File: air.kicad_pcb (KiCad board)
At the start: 2 copper layers, 40.5 x 19.3 mm, 48 parts, among them J1 Conn_01x05, J2 Conn_01x05, J3 Conn_01x04, U2 AIR32F103CBT6-LQFP48, U3 RT9013-33GB, U4 USBLC6-2SC6, Y1 8M/20pF

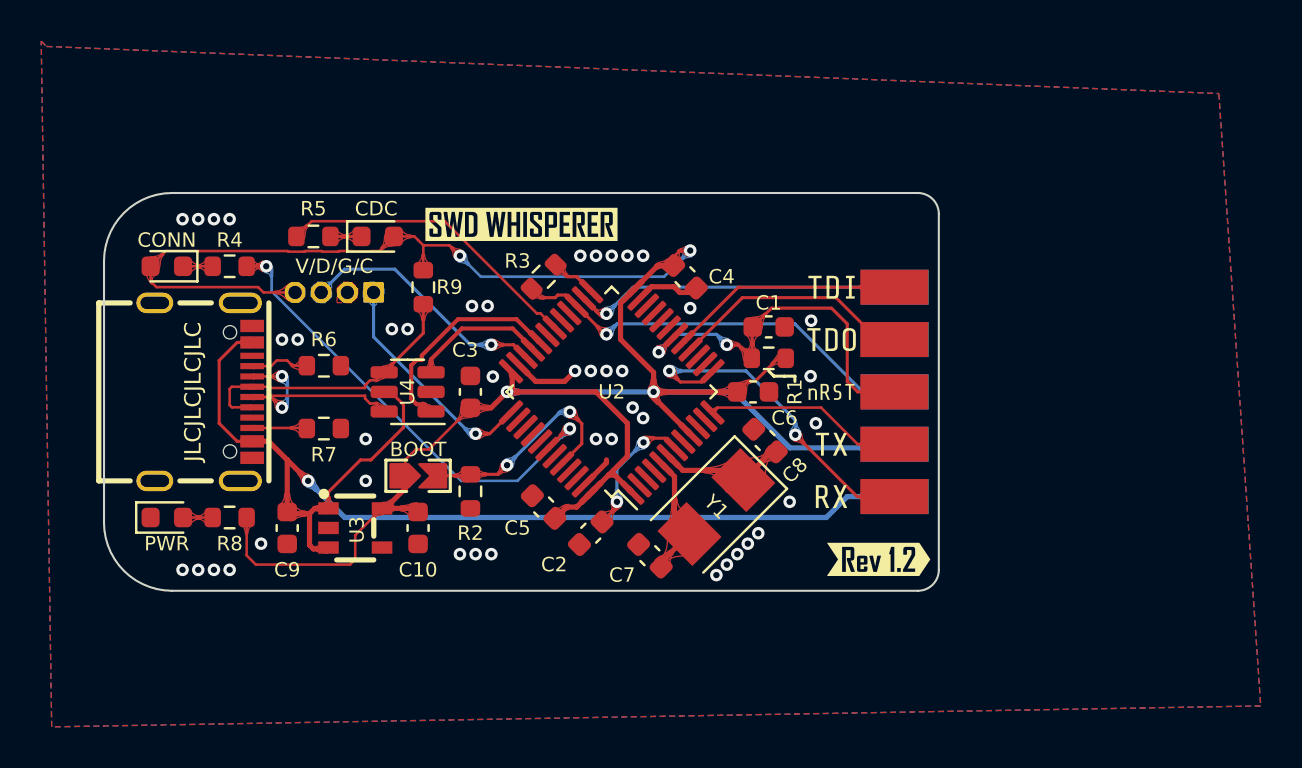
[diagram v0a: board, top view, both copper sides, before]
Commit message: V1.3 3225晶振版本
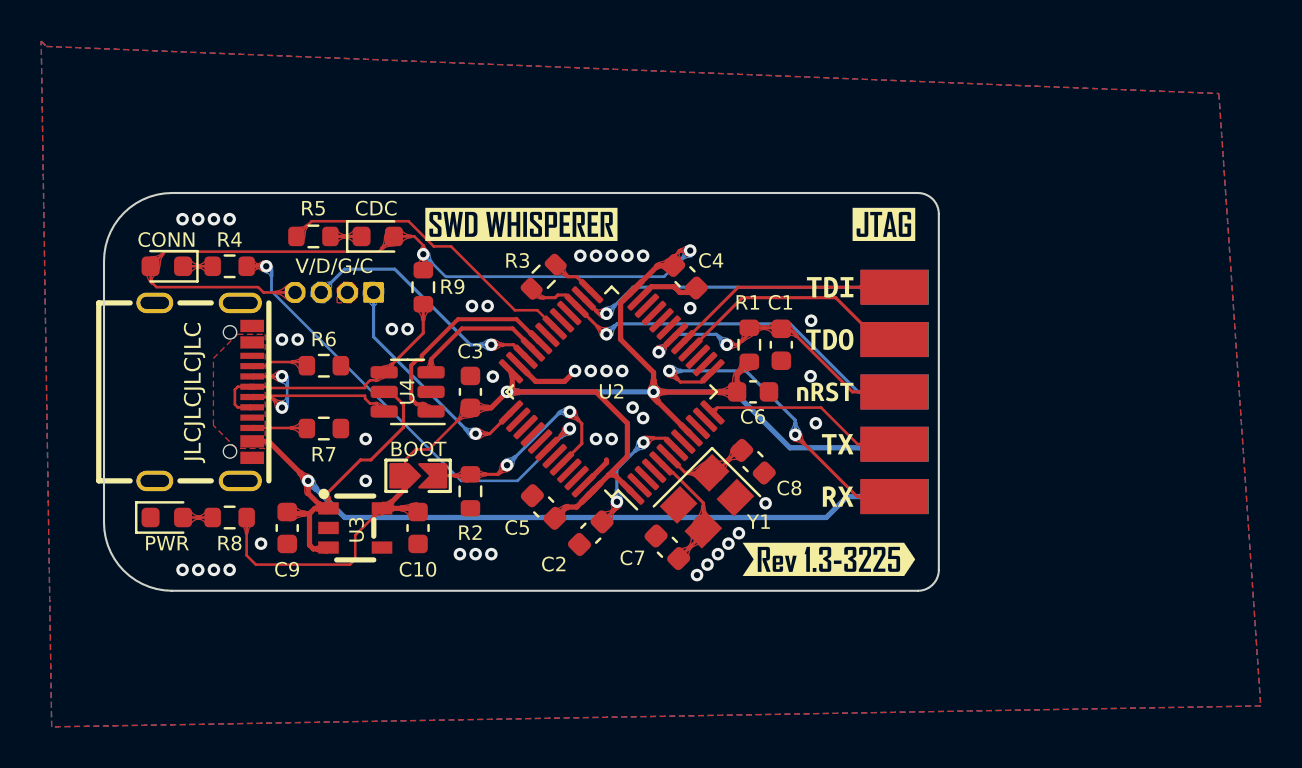
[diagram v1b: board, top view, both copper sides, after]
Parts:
- removed kibuzzard-62F95AB5: G***, kibuzzard-62F95AB5
- removed kibuzzard-62F95AF7: G***, kibuzzard-62F95AF7
- removed kibuzzard-62F95B16: G***, kibuzzard-62F95B16
- removed kibuzzard-62F95C5E: G***, kibuzzard-62F95C5E
- removed kibuzzard-62F95C6D: G***, kibuzzard-62F95C6D
- removed kibuzzard-62F95CA8: G***, kibuzzard-62F95CA8
- removed kibuzzard-62F95CCF: G***, kibuzzard-62F95CCF
- removed kibuzzard-62F95CF5: G***, kibuzzard-62F95CF5
- removed kibuzzard-62F95D14: G***, kibuzzard-62F95D14
- removed kibuzzard-62F95D3A: G***, kibuzzard-62F95D3A
- removed kibuzzard-6300ED64: G***, kibuzzard-6300ED64
- added kibuzzard-6354CCE5: G***, kibuzzard-6354CCE5, B.Cu at (60.9, 61.0)
- added kibuzzard-6354CCEF: G***, kibuzzard-6354CCEF, B.Cu at (61.2, 63.5)
- added kibuzzard-6354CCF5: G***, kibuzzard-6354CCF5, B.Cu at (61.0, 55.9)
- added kibuzzard-6354CD34: G***, kibuzzard-6354CD34, B.Cu at (58.6, 53.3)
- added kibuzzard-6354CD45: G***, kibuzzard-6354CD45, B.Cu at (58.6, 58.4)
- added kibuzzard-6354CD6B: G***, kibuzzard-6354CD6B, F.Cu at (63.5, 50.3)
- added kibuzzard-6354CD83: G***, kibuzzard-6354CD83, F.Cu at (61.3, 61.0)
- added kibuzzard-6354CD88: G***, kibuzzard-6354CD88, F.Cu at (61.3, 63.5)
- added kibuzzard-6354CD9D: G***, kibuzzard-6354CD9D, F.Cu at (60.9, 55.9)
- added kibuzzard-6354CDA6: G***, kibuzzard-6354CDA6, F.Cu at (60.9, 53.3)
- added kibuzzard-6354D1B1: G***, kibuzzard-6354D1B1, F.Cu at (60.8, 66.5)
- added kibuzzard-6354D1FB: G***, kibuzzard-6354D1FB, F.Cu at (60.7, 58.4)
- Y1: footprint Crystal:Crystal_SMD_5032-2Pin_5.0x3.2mm -> Crystal:Crystal_SMD_3225-4Pin_3.2x2.5mm
- moved C8 1.18 mm to (57.1, 61.8), turned to -45 degrees
- moved R1 1.15 mm to (57.0, 56.1), turned to 90 degrees
- moved C1 1.06 mm to (58.5, 56.1), turned to -90 degrees
- moved C7 0.94 mm to (53.0, 66.0)
- moved Y1 0.54 mm to (54.9, 63.7)
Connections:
- Y1 pad 2: OSC_IN -> GND
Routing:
- net +5V: track 55.4 -> 47.8 mm
- net TGT_NREST: track 17.1 -> 14.7 mm
- net OSC_OUT: track 6.23 -> 4.33 mm
- net +3.3V: track 113.9 -> 112.7 mm
- net USB+: track 14.0 -> 13.4 mm
- added copper zone on F.Cu, net +5V

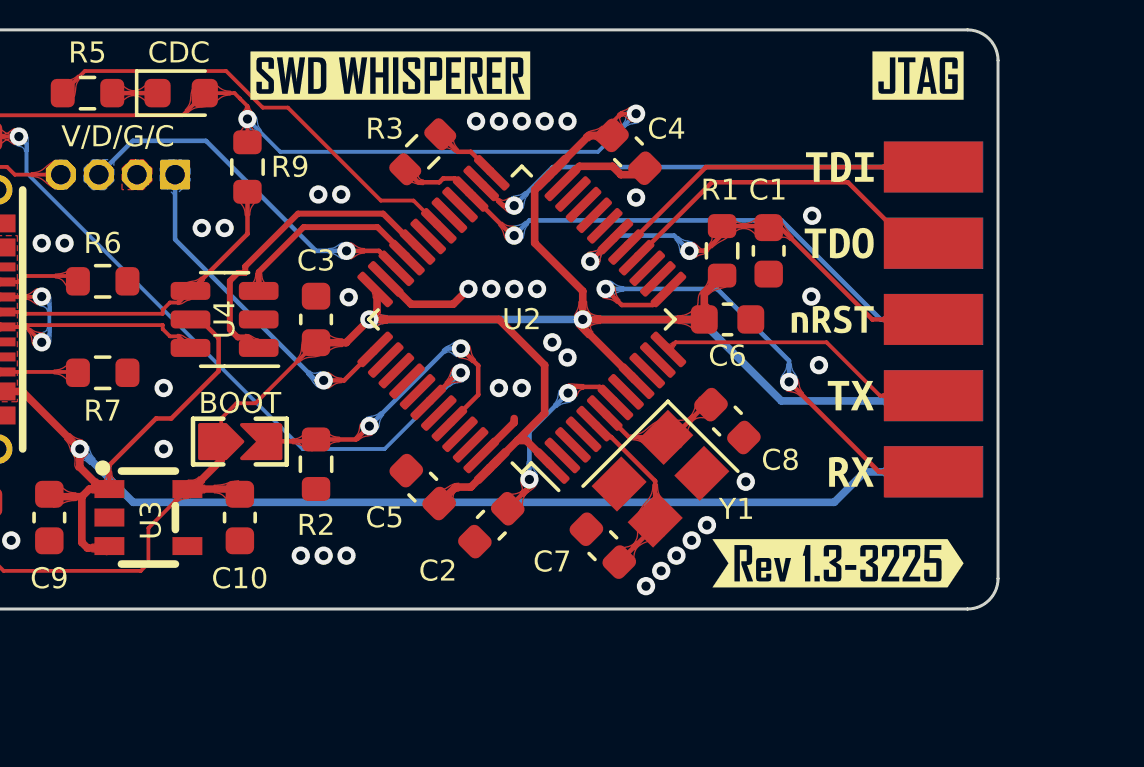
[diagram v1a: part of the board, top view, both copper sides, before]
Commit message: 更新了SWO的硬件功能 从该板开始 可能不兼容上一代的固件
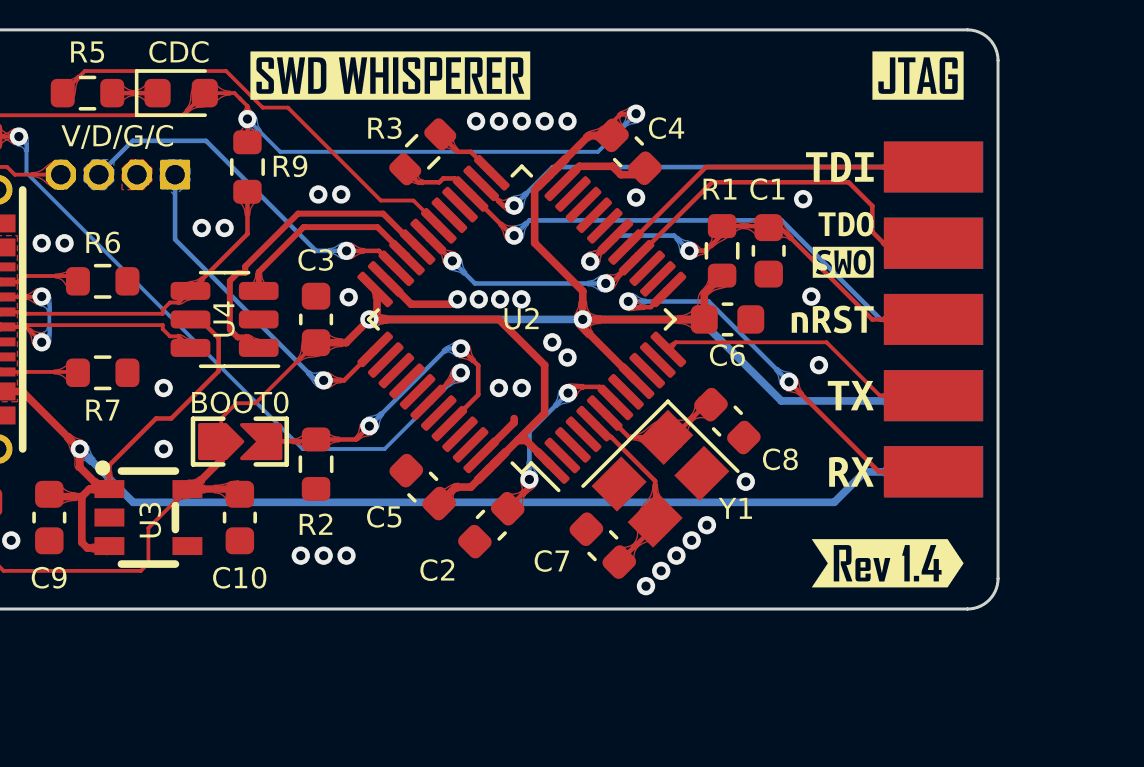
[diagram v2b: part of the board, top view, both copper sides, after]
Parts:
- removed kibuzzard-6354CD9D: G***, kibuzzard-6354CD9D
- removed kibuzzard-6354D1B1: G***, kibuzzard-6354D1B1
- added kibuzzard-637AECBC: G***, kibuzzard-637AECBC, F.Cu at (62.5, 66.5)
- added kibuzzard-637AECE1: G***, kibuzzard-637AECE1, F.Cu at (61.1, 55.2)
- added kibuzzard-637AED1A: G***, kibuzzard-637AED1A, F.Cu at (61.0, 56.5)
- renumbered BOOT to BOOT0
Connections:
- U2 pad 31: unconnected-(U2-Pad31) -> TGT_TDO
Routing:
- net TGT_TDO: track 11.8 -> 20.2 mm, vias 0 -> 2
- net UART_RX: track 16.4 -> 14.2 mm
- net GND: track 8.58 -> 8.07 mm

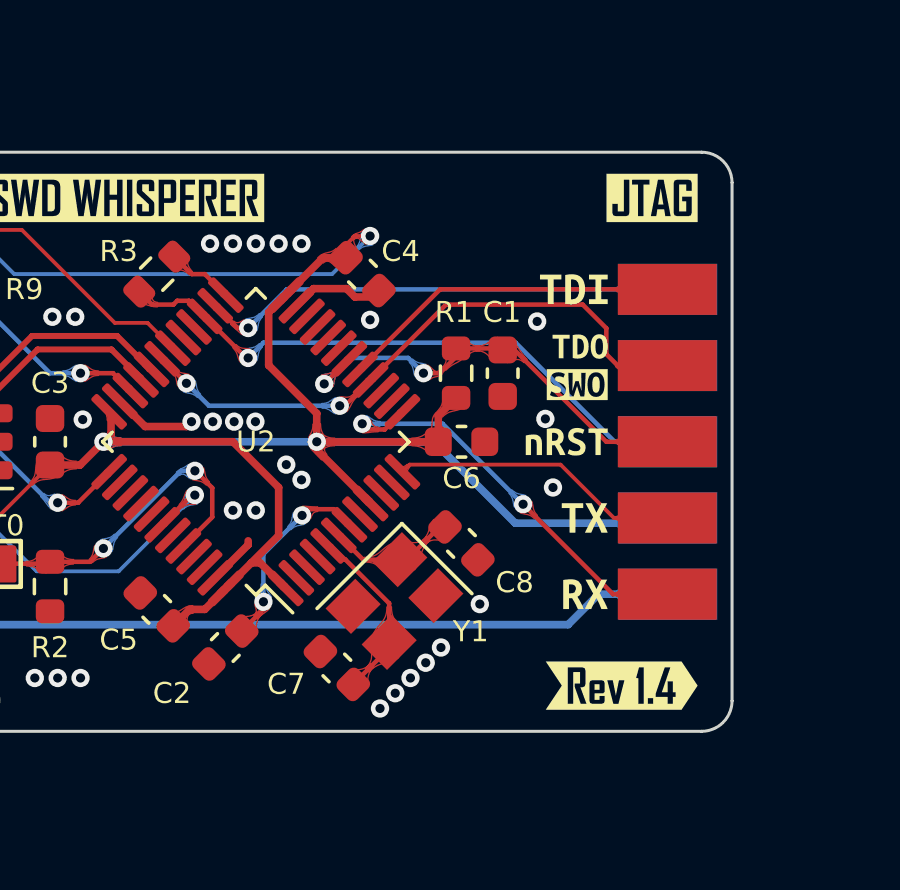
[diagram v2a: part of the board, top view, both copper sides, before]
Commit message: v1.5 added series resistor on debug lines
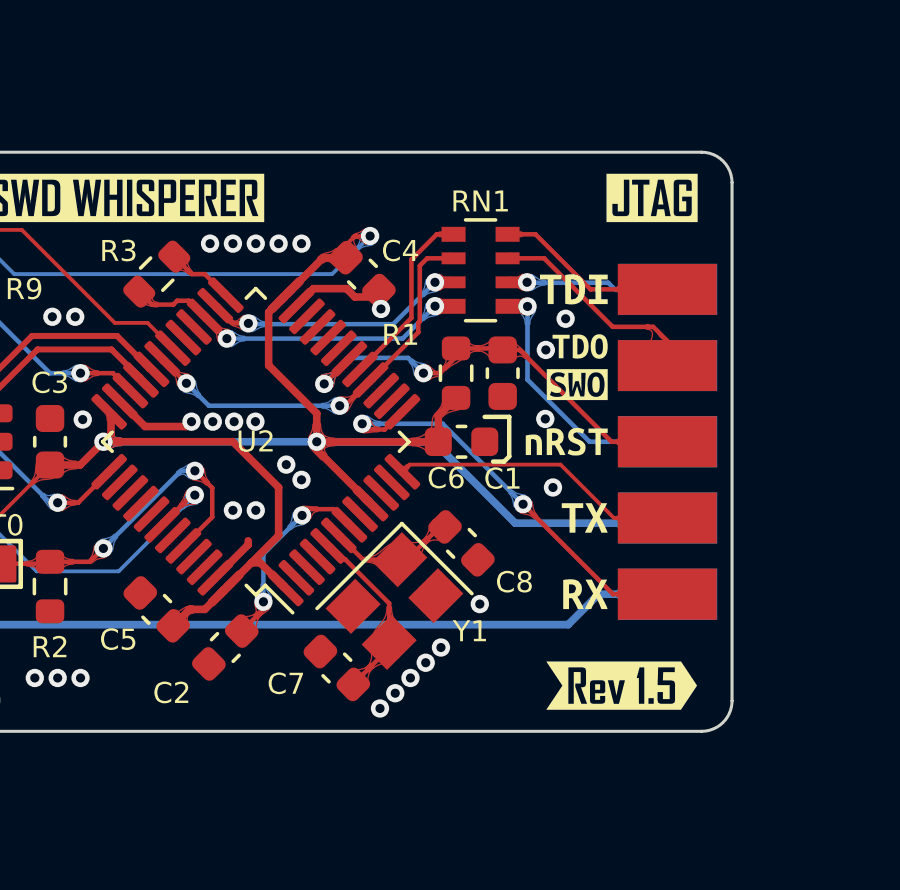
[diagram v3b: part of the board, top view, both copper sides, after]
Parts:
- removed kibuzzard-637AECBC: G***, kibuzzard-637AECBC
- added RN1: 22R, Resistor_SMD:R_Array_Convex_4x0603, F.Cu at (57.8, 52.7)
- added kibuzzard-638212D3: G***, kibuzzard-638212D3, F.Cu at (62.5, 66.5)
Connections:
- R3 pad 1: TGT_SWDIO/TMS -> IN_TGT_SWDIO/TMS
- U2 pad 16: TGT_TDO -> IN_TGT_TDO
- U2 pad 17: TGT_TDI -> IN_TGT_TDI
- U2 pad 26: TGT_SWCLK/TCK -> IN_TGT_SWCLK/TCK
- U2 pad 27: TGT_SWDIO/TMS -> IN_TGT_SWDIO/TMS
- U2 pad 31: TGT_TDO -> IN_TGT_TDO
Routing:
- net IN_TGT_TDO: track 0.00 -> 13.7 mm, vias 0 -> 2
- net TGT_TDO: track 20.2 -> 7.29 mm, vias 2 -> 0
- net IN_TGT_SWDIO/TMS: track 0.00 -> 11.7 mm, vias 0 -> 2
- net TGT_SWDIO/TMS: track 20.2 -> 8.64 mm
- net TGT_SWCLK/TCK: track 15.9 -> 5.44 mm
- net IN_TGT_SWCLK/TCK: track 0.00 -> 8.78 mm, vias 0 -> 2
- net IN_TGT_TDI: track 0.00 -> 6.12 mm
- net TGT_TDI: track 11.3 -> 6.08 mm
- net GND: vias 44 -> 45

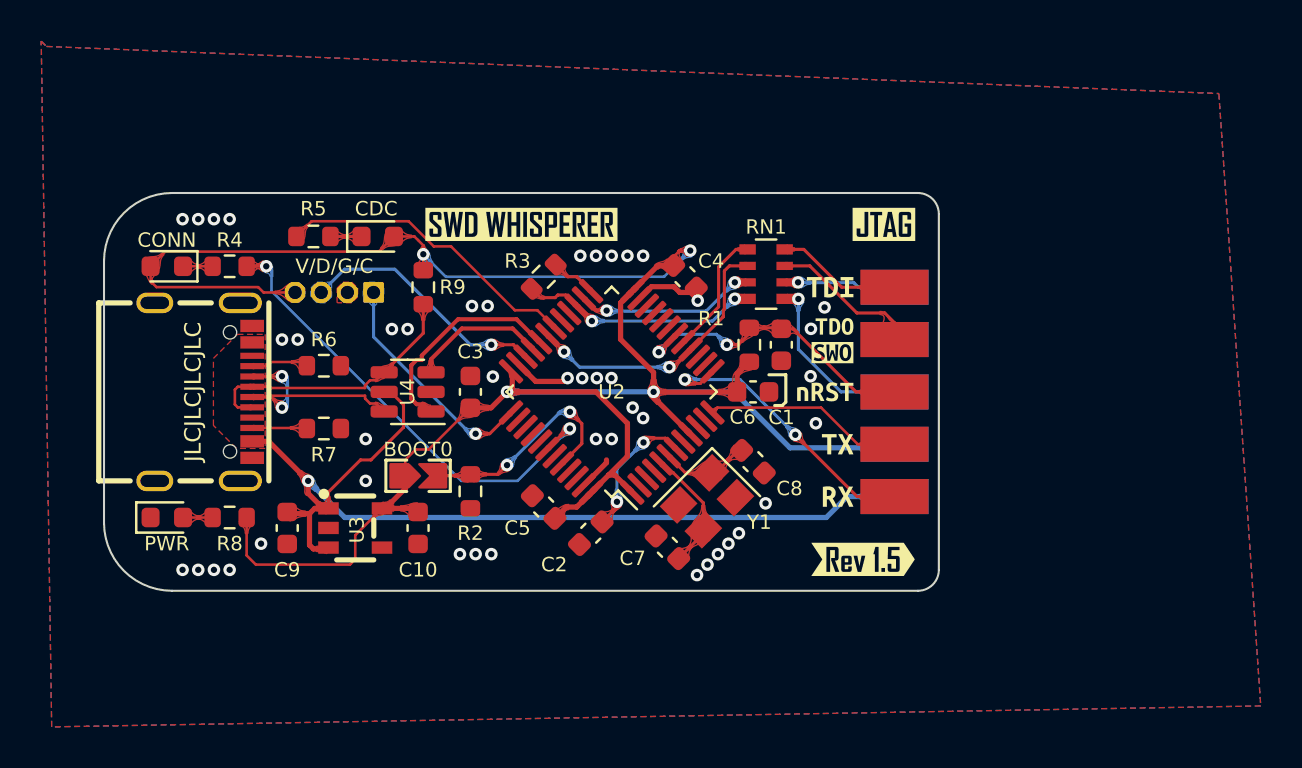
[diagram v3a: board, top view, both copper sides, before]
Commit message: 1.6 Redesign And Add Anti Reverse Current
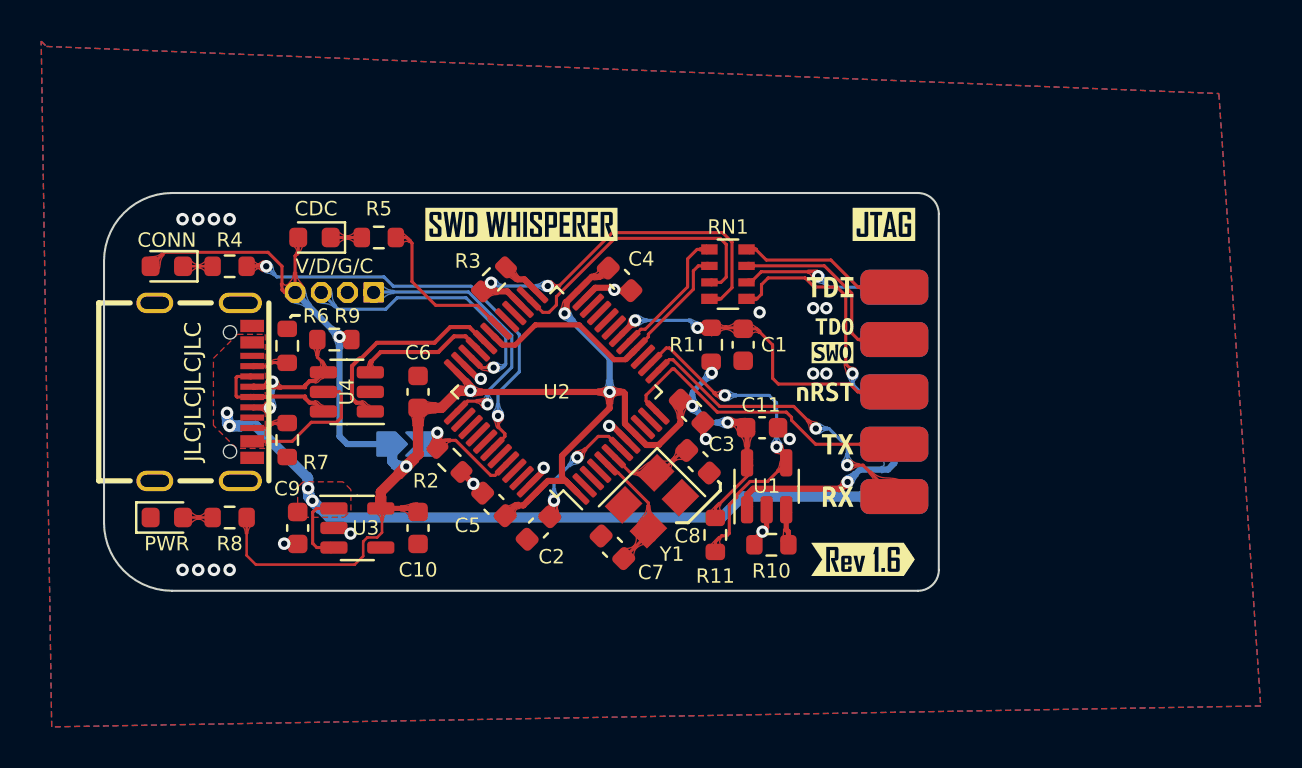
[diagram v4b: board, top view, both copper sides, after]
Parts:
- removed kibuzzard-638212D3: G***, kibuzzard-638212D3
- added C11: 10uF, Capacitor_SMD:C_0603_1608Metric, F.Cu at (57.6, 60.2)
- added R10: 20K, Resistor_SMD:R_0603_1608Metric, F.Cu at (58.0, 65.8)
- added R11: 10K, Resistor_SMD:R_0603_1608Metric, F.Cu at (55.3, 65.4)
- added U1: MT9700, Package_TO_SOT_SMD:SOT-23-5, F.Cu at (57.8, 63.0)
- added kibuzzard-63A8965B: G***, kibuzzard-63A8965B, F.Cu at (62.5, 66.5)
- BOOT0: moved to B.Cu
- U3: footprint Shaojie_Custom:SOT-23-5_L3.0-W1.7-P0.95-LS2.8-BR -> Package_TO_SOT_SMD:SOT-23-5
- moved C6 16.3 mm to (40.9, 58.4), turned to 90 degrees
- moved C3 10.8 mm to (54.2, 59.4), turned to -45 degrees
- moved R9 5.01 mm to (36.8, 55.9), turned to 180 degrees
- moved C4 3.18 mm to (50.7, 53.0)
- moved R5 3.17 mm to (39.0, 50.9), turned to 180 degrees
- moved D2 3.07 mm to (35.9, 50.9), turned to 180 degrees
- moved U4 2.95 mm to (37.4, 58.4)
- moved C7 2.67 mm to (50.3, 66.0)
- moved C8 2.67 mm to (54.5, 61.8)
- moved U2 2.67 mm to (47.6, 58.4)
- moved Y1 2.67 mm to (52.2, 63.7)
- moved C2 2.55 mm to (46.7, 65.0)
- moved R3 2.42 mm to (44.6, 53.0)
- moved C5 2.42 mm to (44.6, 63.9)
- moved R6 2.02 mm to (34.5, 56.2), turned to 90 degrees
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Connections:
- J2 pad 4: +3.3V -> /3.3V_Header
- U2 pad 14: unconnected-(U2-Pad14) -> EN_3.3V
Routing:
- net +3.3V: track 112.7 -> 90.4 mm, vias 4 -> 8
- net EN_3.3V: track 0.00 -> 17.1 mm, vias 0 -> 2
- net /3.3V_Header: track 0.00 -> 9.43 mm, vias 0 -> 1
- net IN_TGT_SWDIO/TMS: track 11.7 -> 19.4 mm
- net TGT_CDC: track 15.0 -> 7.95 mm
- net UART_TX: track 9.66 -> 15.2 mm
- net IN_TGT_SWCLK/TCK: track 8.78 -> 14.2 mm, vias 2 -> 0
- net USB-: track 11.7 -> 6.31 mm, vias 2 -> 0
- net Net-(BOOT0-Pad2): track 11.2 -> 6.30 mm, vias 2 -> 1
- net USB+: track 13.4 -> 8.83 mm, vias 0 -> 2
- net GND: track 8.07 -> 12.4 mm, vias 45 -> 23
- net TGT_SWDIO/TMS: track 8.64 -> 12.5 mm
- net TGT_TDO: track 7.29 -> 9.79 mm
- net TGT_SWCLK/TCK: track 5.44 -> 7.70 mm
- net TGT_CONNECT: track 23.1 -> 21.0 mm
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- removed copper zone on F.Cu, net +3.3V
- removed copper zone on B.Cu, net DBG_SWCLK
- removed copper zone on B.Cu, net DBG_SWDIO

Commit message: still 1.6 but contain some fix to publish work
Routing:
- net GND: vias 23 -> 25
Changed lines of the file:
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@@
   (paper "A4")
   (title_block
-    (date "2022-08-15")
-    (rev "1.1")
+    (title "SWD WHISPERER")
+    (date "2023-02-06")
+    (rev "1.6")
+    (company "[REDACTED]")
   )
   (layers
@@
     (attr board_only exclude_from_pos_files exclude_from_bom)
     (fp_text reference "kibuzzard-63A8965B" (at 0 -3.853656) (layer "F.SilkS") hide
-      (effects (font (size 0 0)))
+      (effects (font (size 0 0) (thickness 0.15)))
     )
     (fp_text value "G***" (at 0 3.853656) (layer "F.SilkS") hide
-      (effects (font (size 0 0)))
+      (effects (font (size 0 0) (thickness 0.15)))
     )
     (fp_poly (pts
@@
   (via (at 37.621 65.295) (size 0.6) (drill 0.3) (layers "F.Cu" "B.Cu") (net 2))
   (via (at 30.226 50.038) (size 0.61) (drill 0.305) (layers "F.Cu" "B.Cu") (free) (net 2))
+  (via (at 33.82 62.24) (size 0.6) (drill 0.3) (layers "F.Cu" "B.Cu") (free) (net 2))
   (via (at 58.928 60.706) (size 0.6) (drill 0.3) (layers "F.Cu" "B.Cu") (net 2))
   (via (at 57.47 54.56) (size 0.6) (drill 0.3) (layers "F.Cu" "B.Cu") (free) (net 2))
@@
   (via (at 29.464 50.038) (size 0.61) (drill 0.305) (layers "F.Cu" "B.Cu") (free) (net 2))
   (via (at 31.75 50.038) (size 0.61) (drill 0.305) (layers "F.Cu" "B.Cu") (free) (net 2))
+  (via (at 33.68 54.58) (size 0.6) (drill 0.3) (layers "F.Cu" "B.Cu") (free) (net 2))
   (via (at 60.071 57.531) (size 0.6) (drill 0.3) (layers "F.Cu" "B.Cu") (free) (net 2))
   (via (at 57.61 65.2) (size 0.6) (drill 0.3) (layers "F.Cu" "B.Cu") (net 2))
